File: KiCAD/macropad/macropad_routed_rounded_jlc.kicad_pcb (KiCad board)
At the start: 2 copper layers, 114.6 x 122.2 mm, 39 parts

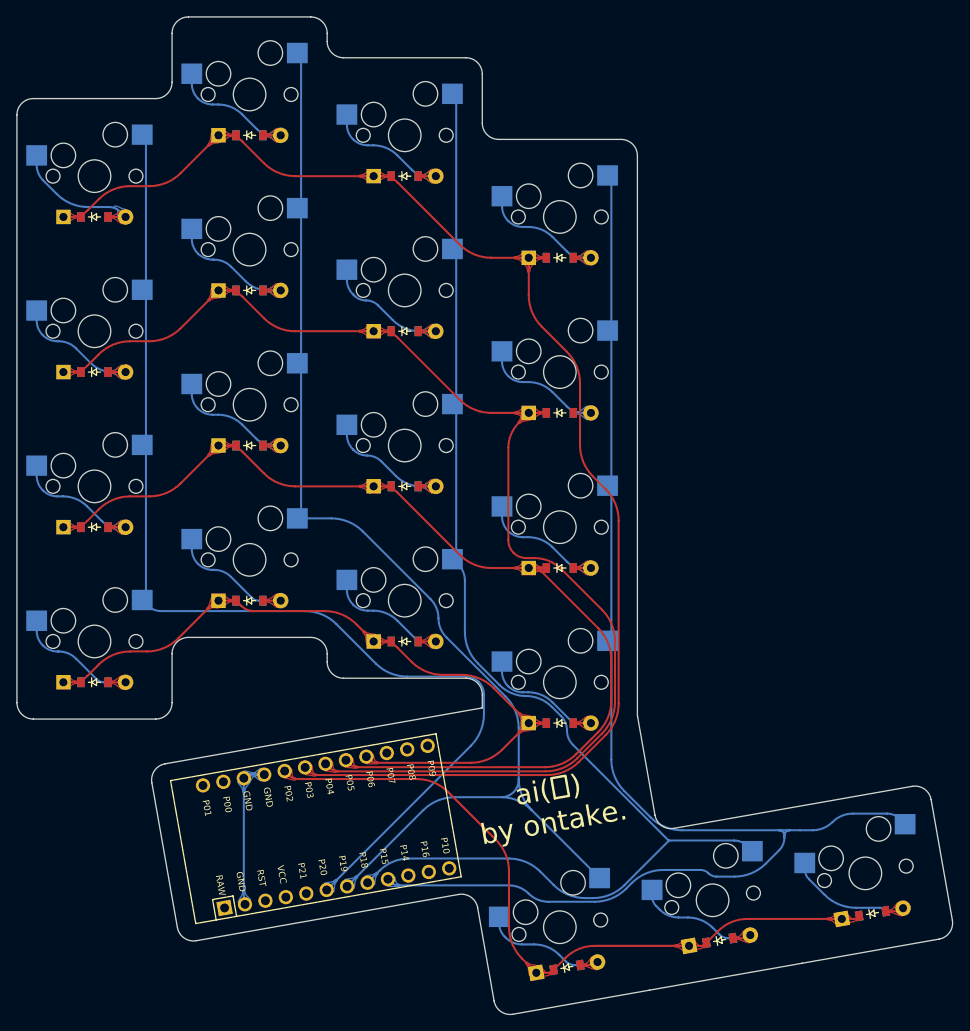
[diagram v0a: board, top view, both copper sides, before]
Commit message: Fix probleme with rounding of the tracks
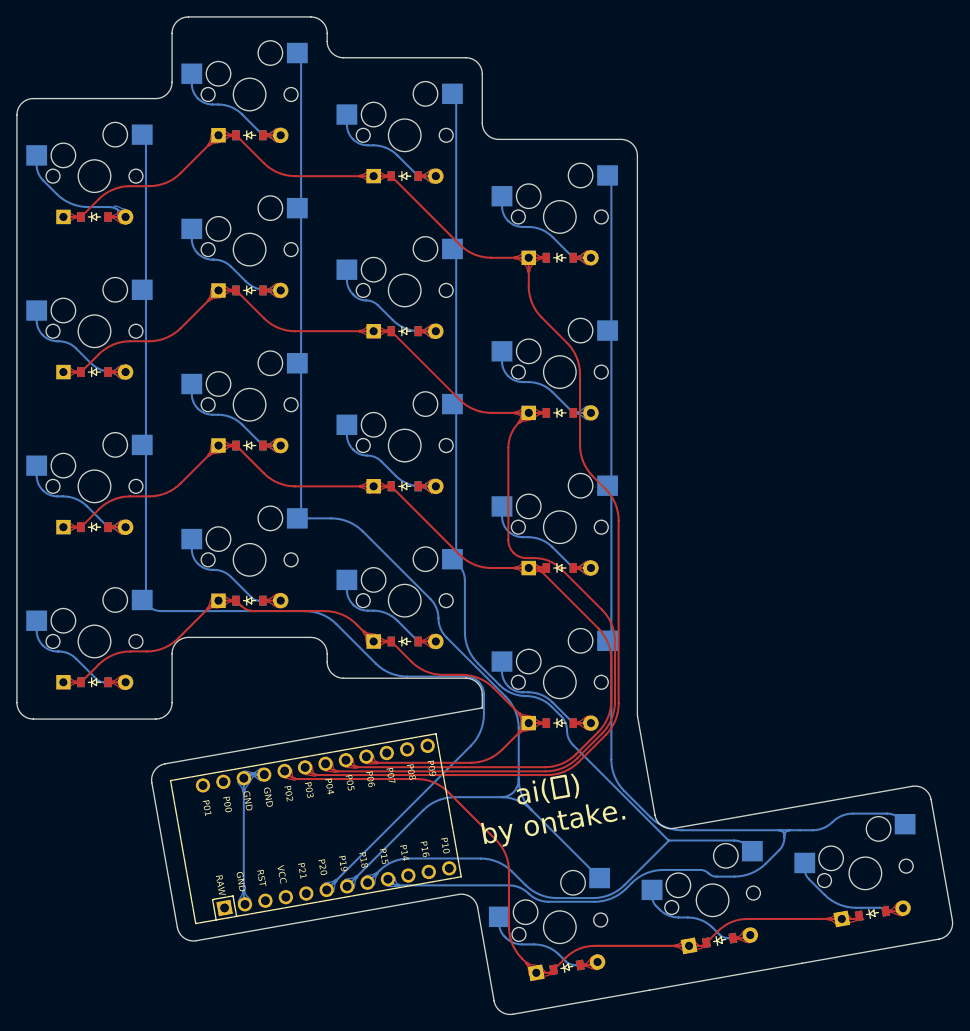
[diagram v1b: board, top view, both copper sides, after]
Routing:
- net P6: track 92.0 -> 90.0 mm
- net P3: track 171.5 -> 169.7 mm
- net P4: track 153.2 -> 151.8 mm
